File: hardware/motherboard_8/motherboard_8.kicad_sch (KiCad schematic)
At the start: 29 parts, among them U1 NC7SVU04P5X, U2 CS48520S, X2 1XXB16368MBA

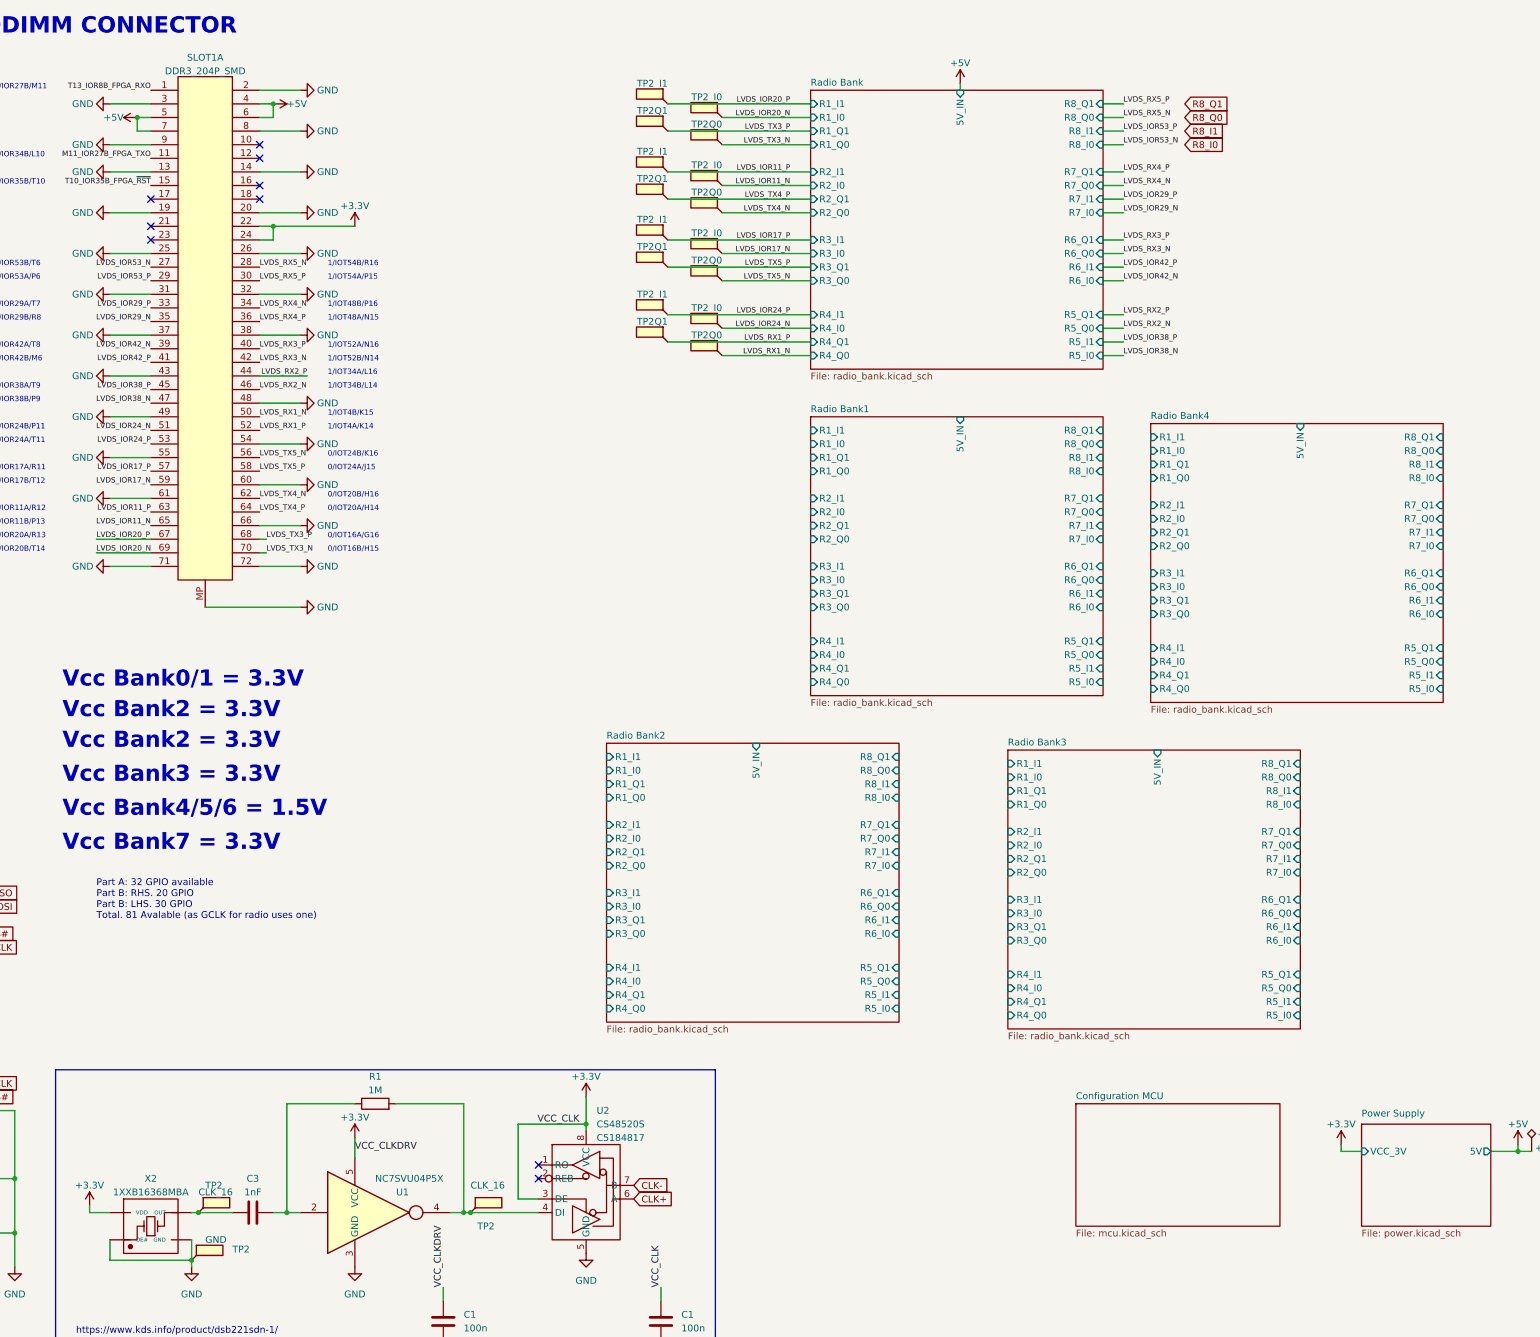
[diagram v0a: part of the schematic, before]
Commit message: Create motherboard 8. Now upgrade number of radios
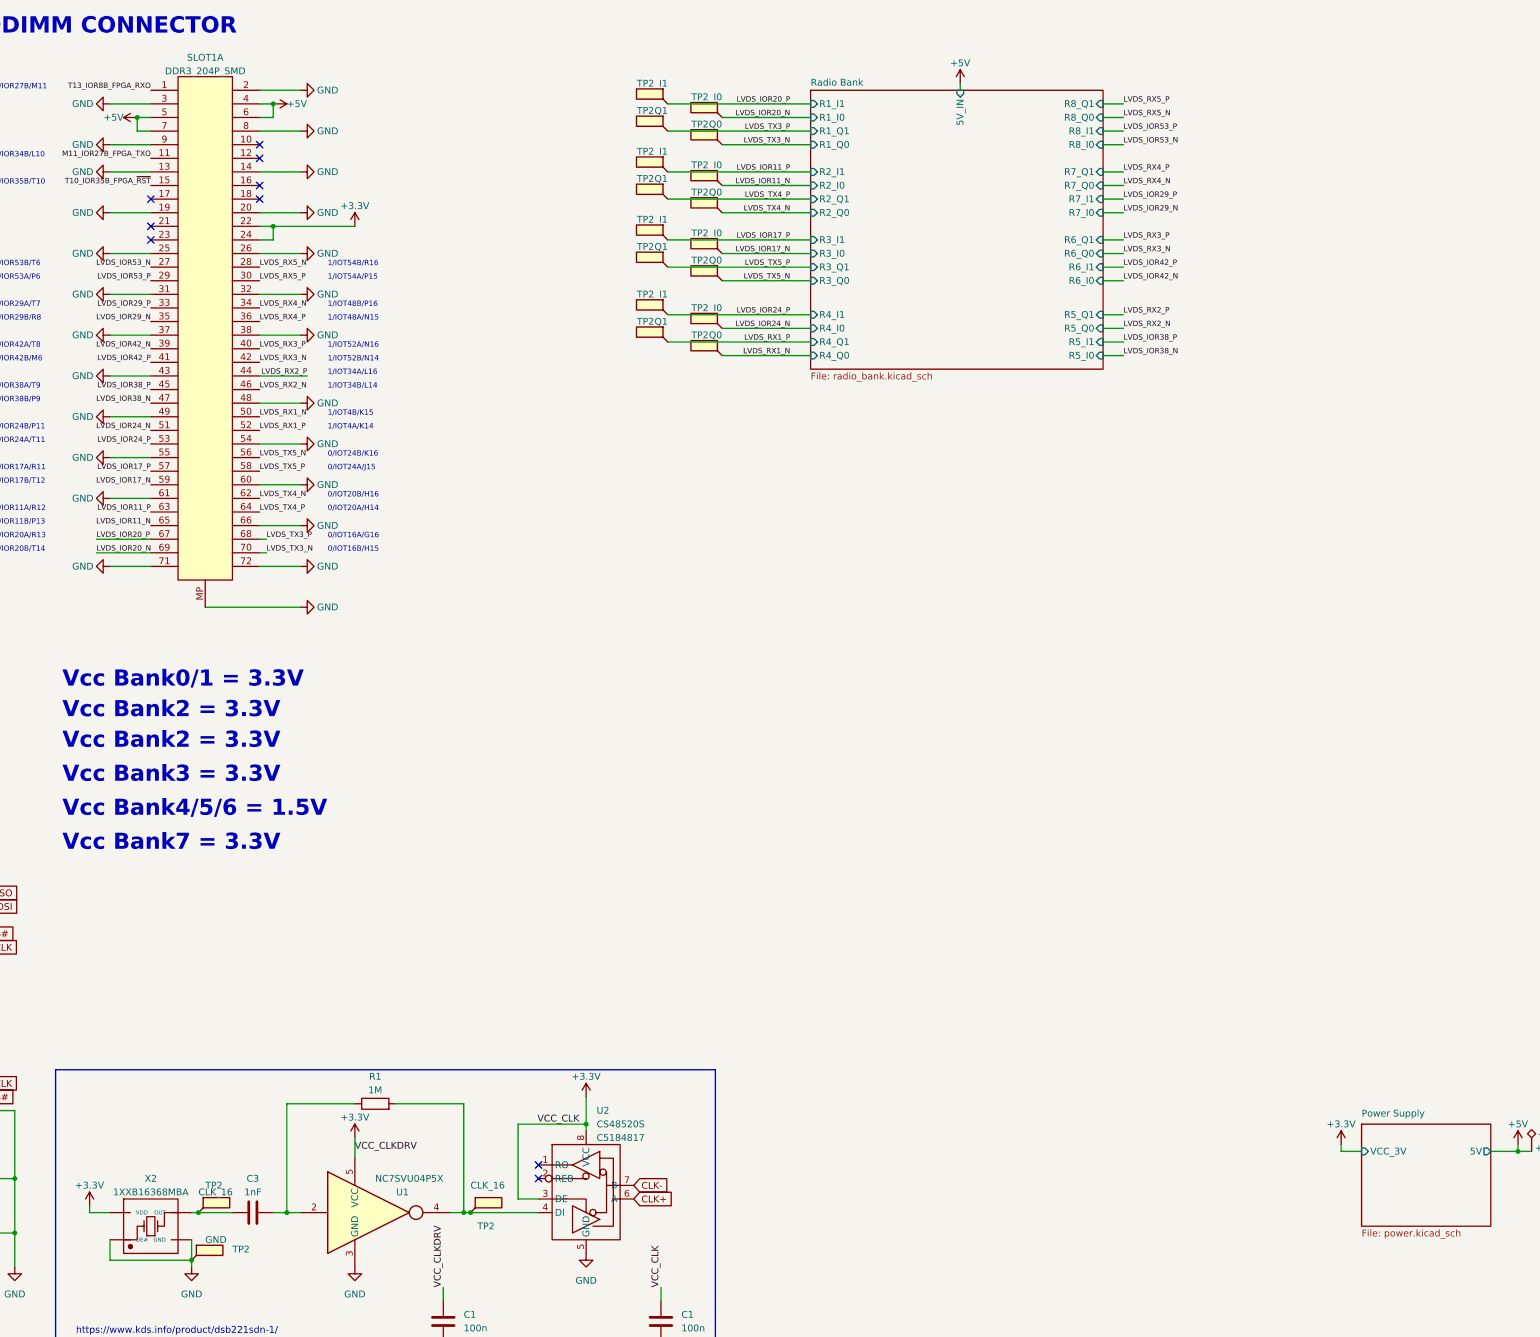
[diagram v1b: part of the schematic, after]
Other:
- removed sheet Configuration MCU
- removed sheet Radio Bank1
- removed sheet Radio Bank2
- removed sheet Radio Bank3
- removed sheet Radio Bank4
- note removed: "Part A: 32 GPIO available Part B: RHS. 20 GPIO Part B: LHS. 30 GPIO Total. 81 Avalable (as GCLK for radio uses one)"
